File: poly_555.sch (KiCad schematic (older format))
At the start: 25 parts, among them U1 LM386

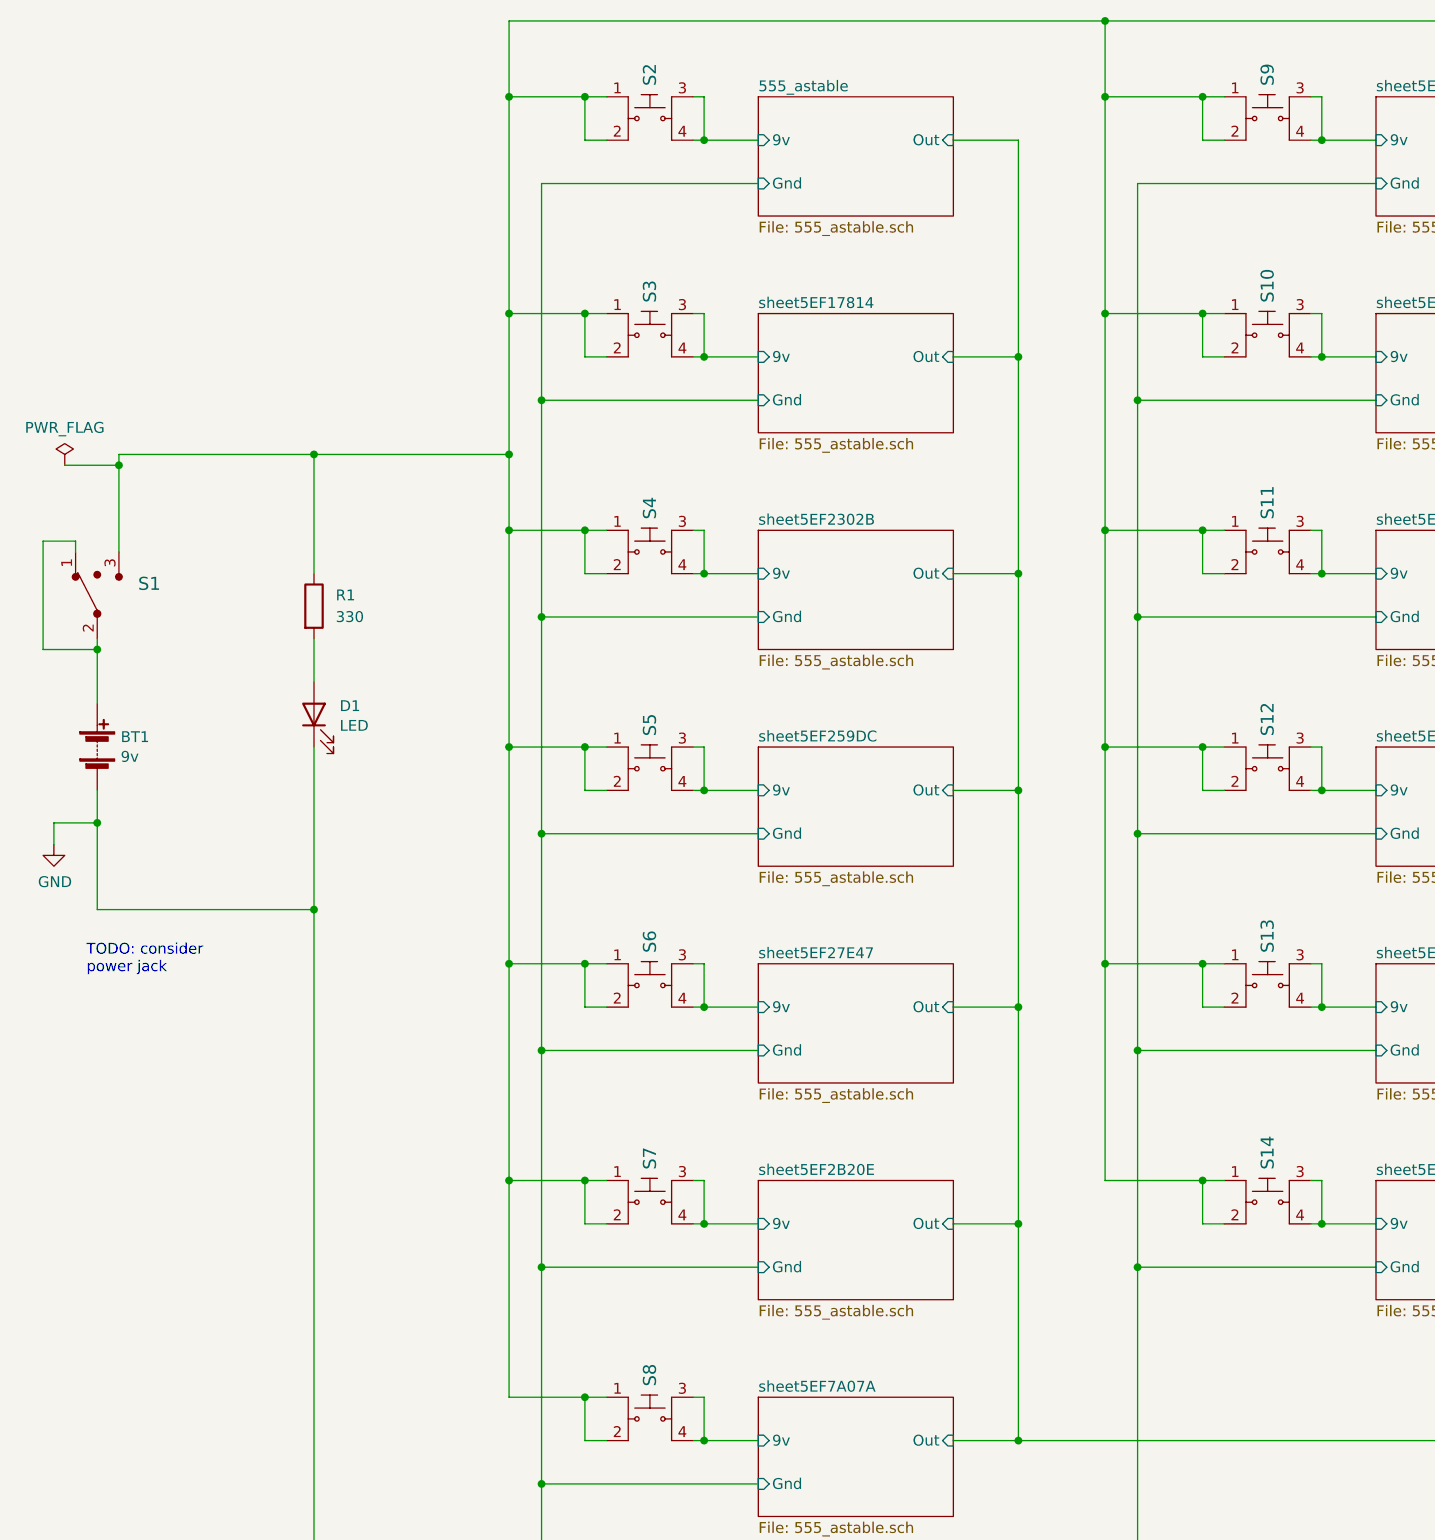
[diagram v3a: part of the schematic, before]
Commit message: Mounting holes
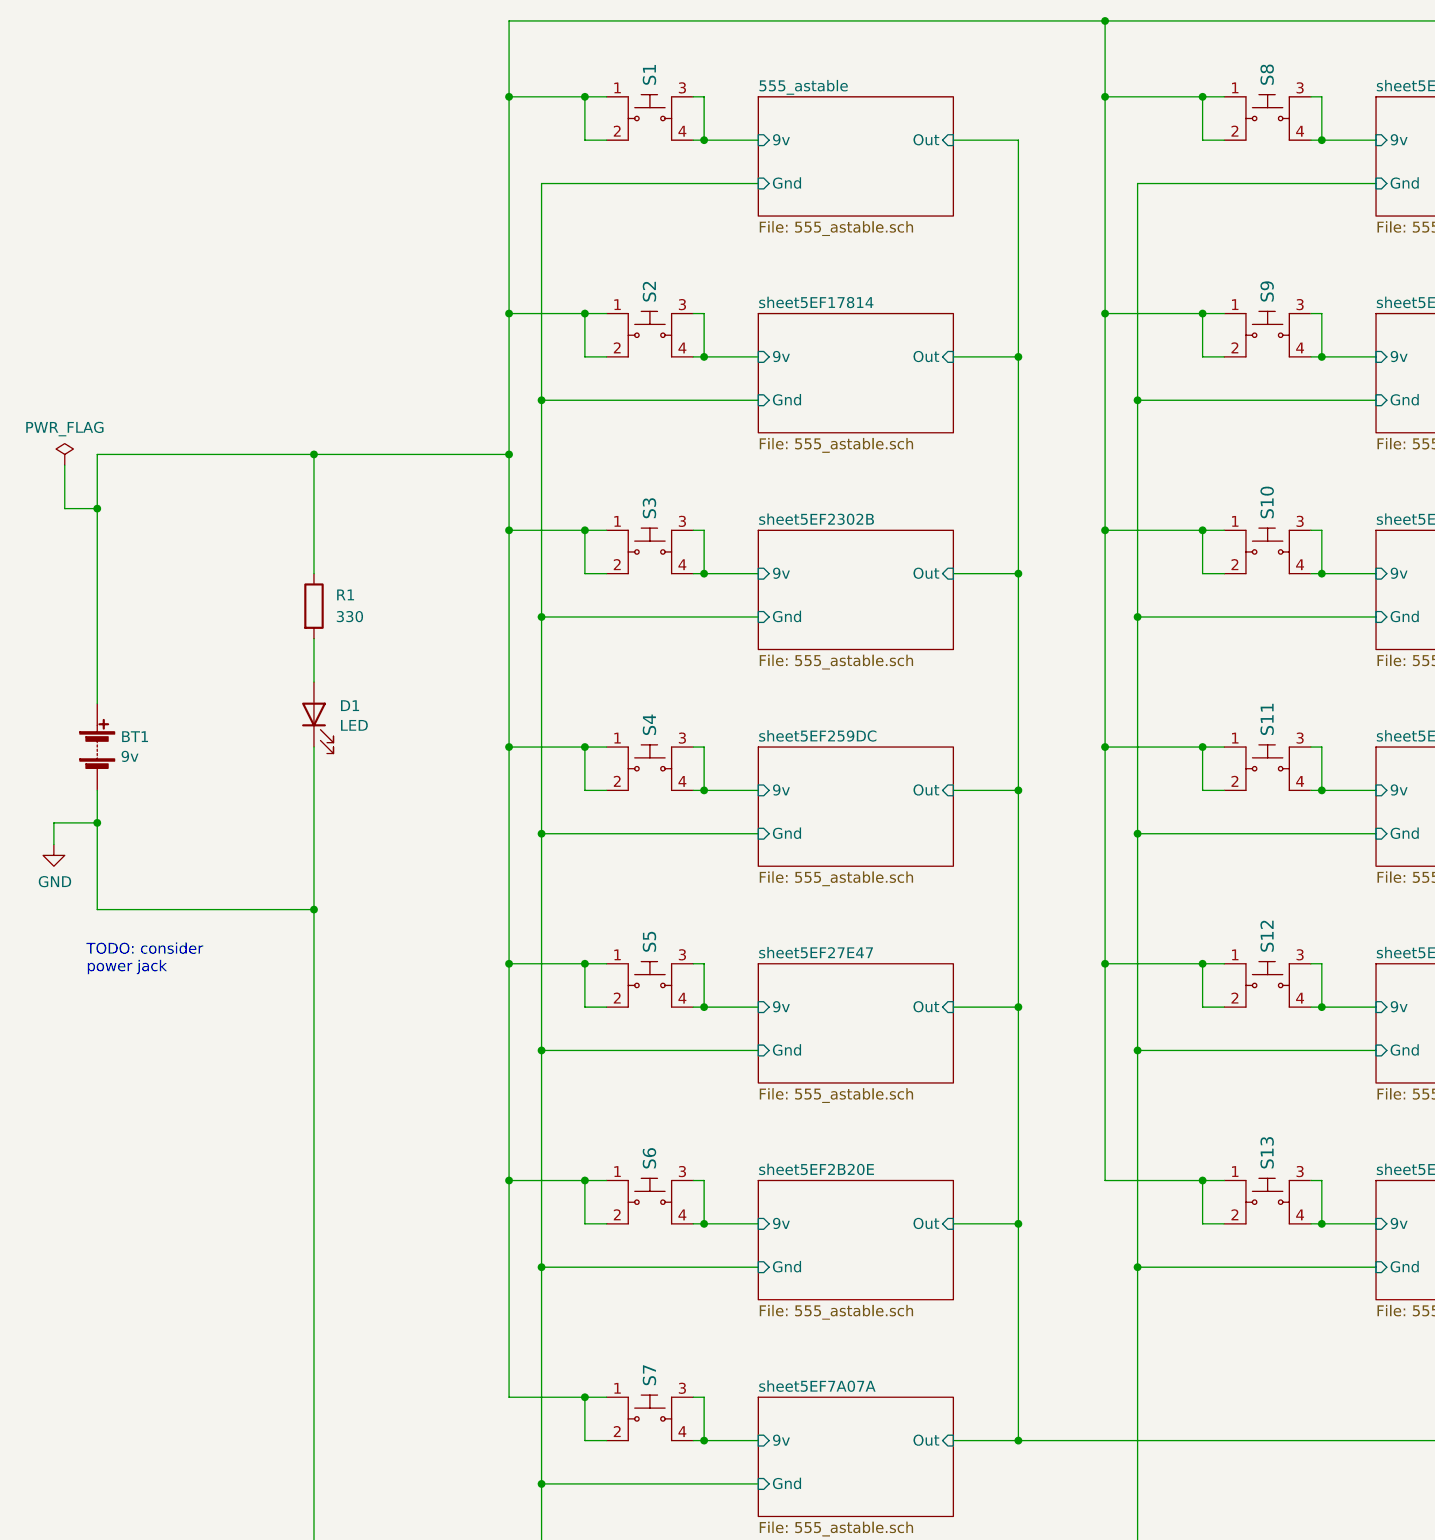
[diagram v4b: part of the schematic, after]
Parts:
- removed S1: 100SP1T1B4M2QE, digikey-footprints:Toggle_Switch_100SP1T1B4M2QE, symbol dk_Toggle-Switches:100SP1T1B4M2QE
- R1: footprint Resistor_THT:R_Axial_DIN0204_L3.6mm_D1.6mm_P7.62mm_Horizontal -> Resistor_THT:R_Axial_DIN0207_L6.3mm_D2.5mm_P2.54mm_Vertical
- RV1: footprint Potentiometer_THT:Potentiometer_Alpha_RD901F-40-00D_Single_Vertical -> Potentiometer_THT:Potentiometer_Bourns_3386F_Vertical
- renumbered S2 to S1, S11 to S10, S12 to S11, S13 to S12, S14 to S13, S3 to S2, S4 to S3, S5 to S4, S6 to S5, S7 to S6, S8 to S7, S9 to S8, S10 to S9
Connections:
- net at BT1.1 (+): now also R1.1, S1.1, S1.2, S10.1, S10.2, S11.1, S11.2, S12.1, S12.2, S13.1, S13.2, S2.1, S2.2, S3.1, S3.2, S4.1, S4.2, S5.1, S5.2, S6.1, S6.2, S7.1, S7.2, S8.1, S8.2, S9.1, S9.2, U1.4 (GND)

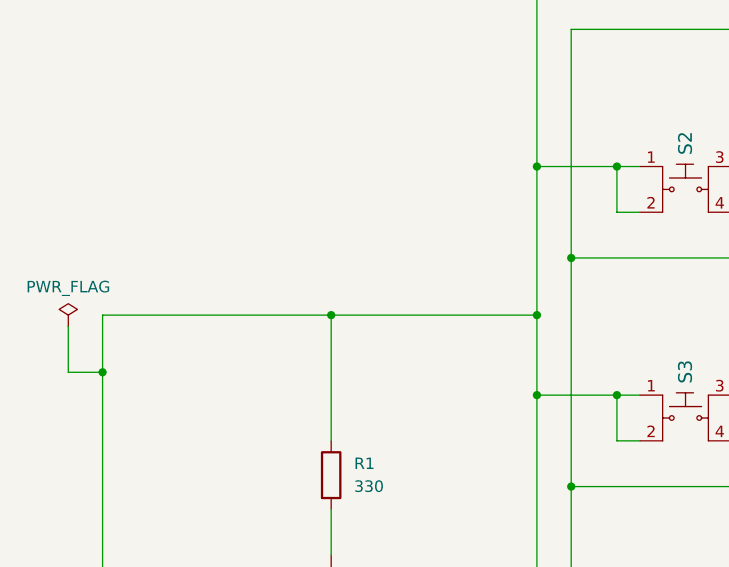
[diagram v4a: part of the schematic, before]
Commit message: TODO power switch
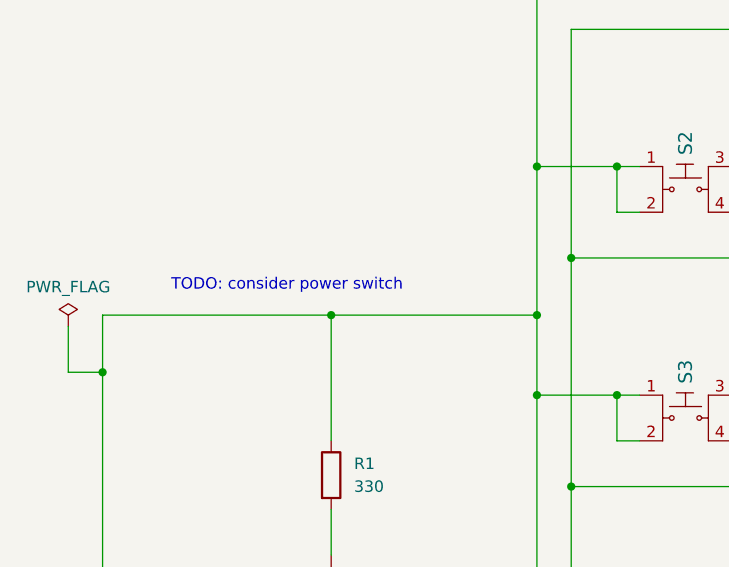
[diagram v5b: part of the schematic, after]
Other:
- note added: "TODO: consider power switch"
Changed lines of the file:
@@
 Wire Wire Line
 	2600 3400 2600 4300
+Text Notes 2900 3050 0    50   ~ 0
+TODO: consider power switch
 $EndSCHEMATC
